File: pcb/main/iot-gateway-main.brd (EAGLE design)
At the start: 100 x 100 mm, 216 parts, among them CON2 6P-SH-TOP, CON3 2P-PH-TOP, J2 DCJACK, Q1 AO3400, Q2 AO3400, Q3 AO3400, Q4 AO3400, T5 BC817, U1 74LVC1G08, U10 CCS811, U11 LT4040, U12 LT8610, U13 LTC2942, U14 FS312F-G, U15 FS8205, U16 MIC23159, U17 ER-TFT035-6-BOT, U18 EFM32GG11B820F2048GQ100, U2 SST26VF064B, U21 74LVC1G04, U3 SST26VF016B, U4 ESP8266EX, U5 RFM69HW, U6 SIM800C, U7 SI7021, U8 SI7210, U9 BMP280, Y1 8 MHz, Y2 32.768 kHz, Y3 24 MHz

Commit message: Big changes to main schematic Finished USB/PD daughter board
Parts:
- removed C73: 100nF, Capacitor:CAP0603
- removed D31: GREEN, LED:0603
- removed D32: RED, LED:0603
- removed J2: DCJACK, DC Jack:DC-050
- removed Q4: AO3400, Alpha Omega:SOT23
- removed R110: 510 Ohms, Resistor:RES0603
- removed R111: 330 Ohms, Resistor:RES0603
- removed T5: BC817, Generic BJT:SOT23
- removed Y1: 8 MHz, Crystal:2-SMD-5032
- removed Y2: 32.768 kHz, Crystal:CM200S
- removed Y3: 24 MHz, Crystal:2-SMD-5032
- added C10, C44, C71: 100nF, Capacitor:CAP0603
- added C45: 1uF, Capacitor:CAP0603
- added C70: 22uF, Capacitor:CAP1206
- added C9: 100uF, Capacitor:CAP1206
- added CON1, CON6: 6P-SH-TOP, JST:SH-06-TOP
- added CON4: 5P-SH-TOP, JST:SH-05-TOP
- added CON5: 3P-SH-TOP, JST:SH-03-TOP
- added D5: RED, LED:1206_REV
- added D6: SMAJ24A, TVS:DO214AC
- added D7: WS2812B, LED:WS2812B-SMD5050
- added LOGO1: OSHW-LOGOM, Silkscreen:OSHW-LOGO-M
- added LOGO2: JS-5MM, Silkscreen:JS_5MM
- added R13: 10K Ohms, Resistor:RES0603
- added R56, R57, R87, R88, R91: 100K Ohms, Resistor:RES0603
- added R65: 71.5K Ohms, Resistor:RES0603
- added R89, R90: 33 Ohms, Resistor:RES0603
- added T1: BC817, Generic BJT:SOT23
- added TP10, TP11, TP12, TP9: TESTPOINT-1.27MM, PADs:PAD1.27MM
- added U19: LTC2942, Analog Devices:DFN6
- added U20: FS8205, Fortune:SOT23-6
- added X1: 8 MHz, Crystal:2-SMD-5032
- added X2: 32.768 kHz, Crystal:2-SMD-3215
- added X3: 26 MHz, Crystal:4-SMD-3225
- C11: value 1nF -> 100nF
- C12: value 100uF -> 100nF; device Capacitor:CAP1206 -> Capacitor:CAP0603
- C14: value 100nF -> 4pF
- C15: value 100nF -> 20pF
- C16: value 100nF -> 4.7pF
- C17: value 4pF -> 20pF
- C18: value 4.7pF -> 100nF
- C19: value 20pF -> 100nF
- C20: value 20pF -> 100uF; device Capacitor:CAP0603 -> Capacitor:CAP1206
- C22, C24: value 100uF -> 33pF; device Capacitor:CAP1206 -> Capacitor:CAP0603
- C23, C42, C43: value 100nF -> 1uF
- C25, C38: value 1uF -> 100nF
- C26, C27: value 33pF -> 100nF
- C29: value 100nF -> 100uF; device Capacitor:CAP0603 -> Capacitor:CAP1206
- C32: value 100uF -> 100nF; device Capacitor:AL-CAP-CASE-D -> Capacitor:CAP0603
- C33, C34: value 4.7uF -> 1nF
- C37: value 10nF -> 100nF
- C39: value 100uF -> 4.7uF; device Capacitor:CAP1206 -> Capacitor:CAP0603
- C40: value 22uF -> 4.7uF; device Capacitor:CAP1206 -> Capacitor:CAP0603
- C41: value 1nF -> 470pF
- C46: value 10pF -> 100uF; device Capacitor:CAP0603 -> Capacitor:CAP1206
- C47: value 100uF -> 10nF; device Capacitor:CAP1206 -> Capacitor:CAP0603
- C48: value 22uF -> 470pF; device Capacitor:CAP1206 -> Capacitor:CAP0603
- C49: value 10uF -> 470pF
- C50, C53, C54, C62: value 100nF -> 470pF
- C52: value 100nF -> 10pF
- C55: value 4.7uF -> 100uF; device Capacitor:CAP0603 -> Capacitor:CAP1206
- C56: value 100nF -> 10uF
- C57: value 10uF -> 22uF; device Capacitor:CAP0603 -> Capacitor:CAP1206
- C58, C59, C64, C65: value 470pF -> 100nF
- C63: device Capacitor:CAP1206 -> Capacitor:AL-CAP-CASE-D
- C66: value 470pF -> 10uF
- C67: value 470pF -> 100uF; device Capacitor:CAP0603 -> Capacitor:CAP1206
- C68: value 470pF -> 22uF; device Capacitor:CAP0603 -> Capacitor:CAP1206
- C69: value 100nF -> 22uF; device Capacitor:CAP0603 -> Capacitor:CAP1206
- C7: value 100nF -> 4.7uF
- CON2: value 6P-SH-TOP -> 2P-PH-TOP; device JST:SH-06-TOP -> JST:PH-02-TOP
- D1: value WS2812B -> BLUE; device LED:WS2812B-SMD5050 -> LED:1206_REV
- D2: value LED1206 -> WHITE; device LED:1206 -> LED:1206_REV
- D3: value LED1206 -> WS2812B; device LED:1206 -> LED:WS2812B-SMD5050
- D4: value SMAJ24A -> LED1206-REV; device TVS:DO214AC -> LED:1206_REV
- E1, E2: device Microstrip Antenna:TRACE_ANTENNA_2.4GHZ_15.2MM -> Antenna:TRACE_ANTENNA_2.4GHZ_15.2MM
- F1: device PTC Fuses:1812 -> PTC Fuses:1206
- L1: value 1.8nH -> 4.7uH
- L2: value 4.7uH -> 1.8nH; device Inductor:IND0606 -> Inductor:IND0603
- L3: value 2.2uH -> 470nH; device Inductor:IND0505 -> Inductor:IND3225
- L4: value 1uH -> 4.7uH; device Inductor:IND0805 -> Inductor:IND0606
- L5: value 470nH -> 1uH; device Inductor:IND3225 -> Inductor:IND0805
- L6: value 4.7uH -> 2.2uH; device Inductor:IND0603 -> Inductor:IND0505
- R1: value 10K Ohms -> 4.7K Ohms
- R10: value 22 Ohms -> 12K Ohms
- R11: value 1 MOhms -> 10K Ohms
- R12, R20: value 10K Ohms -> 330 Ohms
- R14: value 100 Ohms -> 10K Ohms
- R15, R8: value 100K Ohms -> 10K Ohms
- R16: value 0 Ohms -> 200 Ohms
- R18, R33, R36, R4, R6, R7: value 10K Ohms -> 100K Ohms
- R19: value 12K Ohms -> 100K Ohms
- R2: value 330 Ohms -> 4.7K Ohms
- R22, R9: value 10K Ohms -> 0 Ohms
- R23: value 200 Ohms -> 0 Ohms
- R24: value 10K Ohms -> 22 Ohms
- R25, R46: value 100K Ohms -> 22 Ohms
- R27: value 22 Ohms -> 10K Ohms
- R28: value 330 Ohms -> 10K Ohms
- R29: value 22 Ohms -> 100K Ohms
- R3: value 22 Ohms -> 4.7K Ohms
- R32: value 100K Ohms -> 0 Ohms
- R34, R35: value 0 Ohms -> 100K Ohms
- R37: value 10K Ohms -> 1 MOhms
- R38, R77, R78: value 100K Ohms -> 100 Ohms
- R39: value 25m Ohms -> 1 MOhms; device Resistor:RES1206 -> Resistor:RES0603
- R40: value 18.2K Ohms -> 100 Ohms
- R41: value 100K Ohms -> 1 MOhms
- R42: value 1M Ohms -> 100 Ohms
- R43: value 243K Ohms -> 100K Ohms
- R44: value 12m Ohms -> 1K Ohms; device Resistor:RES1206 -> Resistor:RES0603
- R45: value 1.69M Ohms -> 10K Ohms
- R47: value 100K Ohms -> 147K Ohms
- R48: value 324K Ohms -> 21K Ohms
- R49: value 2K Ohms -> 100K Ohms
- R5: value 1K Ohms -> 4.7K Ohms
- R50, R55: value 100 Ohms -> 100K Ohms
- R51: value 1 MOhms -> 100K Ohms
- R52: value 100 Ohms -> 357K Ohms
- R53: value 100 Ohms -> 61.9K Ohms
- R54: value 1 MOhms -> 17.8K Ohms
- R58: value 309K Ohms -> 100K Ohms
- R59: value 71.5K Ohms -> 100K Ohms
- R61: value 178K Ohms -> 100K Ohms
- R62: value 60.4K Ohms -> 1M Ohms
- R63: value 100K Ohms -> 232K Ohms
- R64: value 0 Ohms -> 309K Ohms
- R66: value 100K Ohms -> 510 Ohms
- R67: value 100K Ohms -> 178K Ohms
- R68: value 1K Ohms -> 60.4K Ohms
- R70: value 100K Ohms -> 330 Ohms
- R73: value 357K Ohms -> 100K Ohms
- R74: value 61.9K Ohms -> 2K Ohms
- R76: value 100K Ohms -> 10m Ohms; device Resistor:RES0603 -> Resistor:RES1206
- R79: value 21K Ohms -> 100K Ohms
- R80: value 147K Ohms -> 1.5M Ohms
- R81: value 100K Ohms -> 274K Ohms
- R82: value 100K Ohms -> 25m Ohms; device Resistor:RES0603 -> Resistor:RES1206
- R84, R85: value 100K Ohms -> 4.7K Ohms
- U1: value 74LVC1G08 -> SST26VF064B; device Logic:SC70-5 -> Microchip:WSOIC8
- U10: value CCS811 -> BMP280; device AMS:LGA10 -> Bosch:BMP280
- U11: value LT4040 -> CCS811; device Analog Devices:QFN24_ASYM -> AMS:LGA10
- U12: value LT8610 -> ER-TFT035-6-BOT; device Analog Devices:MSOP16_EP -> BuyDisplay:FPC-50P-TFT-BOT
- U13: value LTC2942 -> 74LVC1G17; device Analog Devices:DFN6 -> Logic:SC70-5
- U14: value FS312F-G -> LT8636; device Fortune:SOT23-6 -> Analog Devices:QFN20_ASYM_CORNER
- U15: value FS8205 -> MIC23159; device Fortune:SOT23-6 -> Microchip:VQFN20
- U16: value MIC23159 -> 74LVC1G04; device Microchip:VQFN20 -> Logic:SC70-5
- U17: value ER-TFT035-6-BOT -> LTC4040; device BuyDisplay:FPC-50P-TFT-BOT -> Analog Devices:QFN24_ASYM
- U18: value EFM32GG11B820F2048GQ100 -> FS312F-G; device EFM32:QFP100 -> Fortune:SOT23-6
- U2: value SST26VF064B -> EFM32GG11B820F2048GQ100; device Microchip:WSOIC8 -> EFM32:QFP100
- U21: value 74LVC1G04 -> LTC4313-1; device Logic:SC70-5 -> Analog Devices:DFN8
- U6: value SIM800C -> 74LVC1G08; device SimCom:SIM800C -> Logic:SC70-5
- U7: value SI7021 -> SIM800C; device Silicon Labs:DFN6 -> SimCom:SIM800C
- U8: value SI7210 -> SI7021; device Silicon Labs:SOT23-5 -> Silicon Labs:DFN6
- U9: value BMP280 -> SI7210; device Bosch:BMP280 -> Silicon Labs:SOT23-5
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- renumbered U$1 to LOGO3
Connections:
- removed net 12V0: C32.1, C33.1, C36.1, D4.C, F1.1, R80.2, U12.4, U12.5, U12.6
- removed net 12V0_UNFUSED: F1.2, J2.C, J2.C'
- removed net 12V0_VSENSE: C64.1, R79.2, R80.1
- removed net 5V0_NBU_NSENS_SYNC: R78.2, U12.1
- removed net I2C1_SCL_TFT: R7.1, U17.44
- removed net I2C1_SDA_TFT: R6.1, U17.45
- removed net US1_CLK_TFT: U17.36
- removed net US1_CS_TFT: R66.1, U17.38
- removed net US1_MISO_TFT: U17.33
- removed net US1_MOSI_TFT: U17.34
- removed net US2_CTS_GSM: U6.4
- removed net US2_RTS_GSM: U6.3
- removed net US2_RX_GSM: U6.1
- removed net US2_TX_GSM: U6.2
- removed net VIN_DET: J2.DT, R41.1
- removed net WIFI_XTAL_IN: C19.2, U4.28, Y3.1
- removed net WIFI_XTAL_OUT: C20.2, U4.27, Y3.2
- new net !BAT_CHRG_EN: R88.1, U17.4
- new net !FUEL_GAUGE_IRQ: R79.1, U19.5
- new net !US2_CS_TFT: R34.1, U12.38
- new net !USB_PD_IRQ: CON6.2, R83.1
- new net !USB_VBUS_HV_EN: CON4.3
- new net DCJACK_DET: CON6.5, R69.1
- new net I2C1_SCL_SYS: R5.1, U12.44, U19.3, U21.3
- new net I2C1_SDA_SYS: R3.1, U12.45, U19.4, U21.6
- new net I2C_SCL_USB_PD: CON6.3, R85.1, U21.2
- new net I2C_SDA_USB_PD: CON6.4, R84.1, U21.7
- new net N$32: TP11.TP, U7.12
- new net N$55: TP10.TP, U7.11
- new net N$56: TP8.TP, U7.10
- new net N$60: TP5.TP, U7.9
- new net N$61: C15.1, U4.28, X3.2
- new net N$62: C17.1, U4.27, X3.4
- new net N$63: CON5.2, R90.2
- new net N$64: CON5.1, R89.2
- new net U0_CTS_GSM: U7.4
- new net U0_RTS_GSM: U7.3
- new net U0_RX_GSM: U7.1
- new net U0_TX_GSM: U7.2
- new net US2_CLK_TFT: U12.36
- new net US2_MISO_TFT: U12.33
- new net US2_MOSI_TFT: U12.34
- new net USB_D+: R89.1
- new net USB_D-: R90.1
- new net USB_PD_I2C_EN: R87.2, U21.1
- new net USB_PD_I2C_READY: R86.1, U21.5
- new net USB_VBUS_HV_STAT: CON4.2, R91.1
- new net USB_VBUS_SUP_EN: CON4.4
- new net VIN: C40.1, C42.1, C43.1, C63.1, D6.C, F1.1, R47.2, U14.11, U14.14, U14.6
- new net VIN_UNFUSED: CON3.1, F1.2
- new net VIN_VSENSE: C41.1, R47.1, R48.2
- net !5V0_BACKUP: now also R71.1, U16.2, U17.20; no longer R72.1, U11.20, U21.2
- net !BAT_CHRG: now also R75.1, U17.8; no longer R63.1, U11.8
- net !BAT_FAULT: now also R73.1, U17.9; no longer R67.1, U11.9
- net !CCS811_IRQ: now also R29.1, U11.3; no longer R38.1, U10.3
- net !CCS811_RESET: now also R27.1, U11.2; no longer R36.1, U10.2
- net !CCS811_WAKE: now also R28.1, U11.7; no longer R37.1, U10.7
- net !GSM_DTR: now also U7.6; no longer U6.6
- net !GSM_RING: now also U7.7; no longer U6.7
- net !RESET: now also R6.1, U2.36; no longer R69.1, U18.36
- net !TFT_RESET: now also R33.1, U12.10; no longer R32.1, U17.10
- net !TFT_TOUCH_IRQ: now also R36.1, U12.46; no longer R47.1, U17.46
- net !TFT_TOUCH_RESET: now also R35.1, U12.47; no longer R46.1, U17.47
- net !UI_BTN1: now also C33.1, R37.1, R38.2; no longer C41.1, R54.1, R55.2
- net !UI_BTN2: now also C34.1, R39.1, R40.2; no longer C35.1, R51.1, R52.2
- net !UI_BTN3: now also C35.1, R41.1, R42.2; no longer C11.1, R11.1, R14.2
- net !WIFI_RESET: now also CON1.1, R11.1; no longer CON2.1, R18.1
- net 1V8: now also C7.1, L1.1, U2.58; no longer C34.1, L6.1, U18.58
- net 3V3: now also C10.1, C11.1, C18.1, C25.1, C26.1, C27.1, C32.1, C56.1, C61.1, C71.1, C9.1, CON6.1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; no longer C14.1, C15.1, C16.1, C22.1, C52.1, C53.1, C54.1, C57.1, C73.1, L4.2, R15.2, R20.2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
- net 3V3_FB: now also R64.1, R65.2, U15.11; no longer R58.1, R59.2, U16.11
- net 3V3_PGOOD: now also R59.1, U15.12; no longer R60.1, U16.12
- net 4V2: now also C19.1, C20.1, C44.1, C46.1, L3.1, R50.2, R52.2, U15.17, U7.34, U7.35; no longer C23.1, C24.1, C62.1, C63.1, L5.1, R73.2, R82.2, U16.17, U6.34, U6.35
- net 4V2_EN: now also R49.2, U15.18; no longer R76.2, U16.18
- net 4V2_FB: now also R52.1, R53.2, U15.16; no longer R73.1, R74.2, U16.16
- net 4V2_PGOOD: now also R56.1, U15.15; no longer R75.1, U16.15
- net 4V2_VSENSE: now also C48.1, R50.1, R51.2; no longer C65.1, R81.2, R82.1
- net 5V0: now also C36.1, C37.1, C38.1, C39.1, C58.1, C67.1, C68.1, C70.1, CON4.1, D3.1, D7.1, Q3.3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; no longer C47.1, C48.1, C55.1, C56.1, C61.1, C7.1, D1.1, Q1.3, R45.2, R5.2, R84.2, U11.1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
- net 5V0_FB: now also R80.1, R81.2, U17.10, U17.18; no longer R45.1, R48.2, U11.10, U11.18
- net 5V0_ISENSE: now also C62.1, U17.3; no longer C68.1, U11.3
- net 5V0_NBU: now also Q3.2, R76.1, U17.7; no longer Q1.2, R44.1, U11.7
- net 5V0_NBU_NSENS: now also C52.1, C55.1, C57.1, C59.1, L4.2, R62.2, R66.2, R67.2, R76.2, U14.2, U17.16, U17.6; no longer C39.1, C40.1, C42.1, C46.1, L2.2, R110.2, R42.2, R44.2, R61.2, U11.16, U11.6, U12.14
- net 5V0_NBU_NSENS_FB: now also C52.2, R62.1, R63.2, U14.19, U14.20; no longer C46.2, R42.1, R43.2, U12.16
- net 5V0_NBU_NSENS_PGOOD: now also R55.1, U14.1; no longer R77.1, U12.15
- net 5V0_PGOOD: now also R72.1, U17.11; no longer R71.1, U11.11
- net 5V0_VSENSE: now also C50.1, R57.1, R58.2; no longer C66.1, R83.2, R84.1
- net GBAT: now also C64.2, CON2.2, U18.6, U19.2, U20.3; no longer C51.2, CON3.2, U13.2, U14.6, U15.3
- net GND: now also C10.2, C14.1, C16.1, C17.2, C18.2, C19.2, C20.2, C43.2, C44.2, C45.2, C46.2, C70.2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; no longer C14.2, C16.2, C17.1, C18.1, C19.1, C20.1, C52.2, C64.2, C73.2, CON2.6, D1.3, D31.1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
- net GSM_LED_EN: now also U6.2; no longer U1.2
- net GSM_PWRKEY: now also R21.2; no longer R33.2
- net GSM_RF_SYNC: now also U7.29; no longer U6.29
- net GSM_STATUS: now also U7.42; no longer U6.42
- net I2C0_SCL_SENS: now also R2.1, U10.4, U11.10, U8.6, U9.3; no longer R4.1, U10.10, U7.6, U8.3, U9.4
- net I2C0_SDA_SENS: now also U10.3, U11.9, U9.1; no longer U10.9, U7.1, U9.3
- net LED_DI: now also R43.2, U13.2; no longer R10.2
- net MAG_ALERT: now also U9.5; no longer U8.5
- net MAIN_HFXTAL_N: now also X1.1; no longer Y1.1
- net MAIN_HFXTAL_P: now also X1.2; no longer Y1.2
- net MAIN_LFXTAL_N: now also X2.2; no longer Y2.4
- net MAIN_LFXTAL_P: now also X2.1; no longer Y2.1
- net N$1: now also U11.4, U11.5; no longer U10.4, U10.5
- net N$10: now also R9.1; no longer R16.1
- net N$12: now also R54.2, U14.17; no longer R40.2, U12.3
- net N$13: now also C47.1, U14.18; no longer C37.1, U12.2
- net N$14: now also C45.1, U14.15, U14.3; no longer C38.1, U12.13
- net N$15: now also C51.1, L4.1, U14.10, U14.8, U14.9; no longer C43.1, L2.1, U12.10, U12.11, U12.9
- net N$16: now also D2.C, R20.2; no longer D2.1, R28.2
- net N$17: now also D2.A, U6.4; no longer D2.2, U1.4
- net N$18: now also R26.1; no longer R27.1
- net N$19: now also D3.4, U13.4; no longer D1.4, Q4.3, R5.1
- net N$2: now also U7.32; no longer U6.32
- net N$20: now also R22.1, R23.2, U7.20; no longer R34.1, R35.2, U6.20
- net N$21: now also R22.2; no longer R34.2
- net N$22: now also R23.1; no longer R35.1
- net N$23: now also TP1.TP, U7.28; no longer TP8.TP, U6.28
- net N$24: now also Q1.1; no longer Q3.1
- net N$25: now also TP9.TP, U7.26; no longer TP1.TP, U6.26
- net N$26: now also TP6.TP, U7.25; no longer TP2.TP, U6.25
- net N$27: now also T1.3, U7.39; no longer T5.3, U6.39
- net N$28: now also R21.1, T1.1; no longer R33.1, T5.1
- net N$29: now also D1.C, R12.2; no longer D3.1, R2.2
- net N$3: now also R25.1; no longer R26.1
- net N$30: now also U7.24; no longer U6.24
- net N$31: now also TP2.TP, U7.40; no longer TP5.TP, U6.40
- net N$33: now also Q1.3, R32.1; no longer Q3.3, R64.1
- net N$34: now also R45.2, R46.2; no longer R3.2, R9.2
- net N$35: now also R44.1; no longer R68.1
- net N$36: now also C51.2, U14.7; no longer C43.2, U12.12
- net N$37: now also Q3.1, U17.15; no longer Q1.1, U11.15
- net N$38: now also L6.1, U17.21, U17.22; no longer L3.1, U11.21, U11.22
- net N$39: now also R24.2; no longer R29.2
- net N$4: now also U6.1, U7.41; no longer U1.1, U6.41
- net N$40: now also R74.2, U17.2; no longer R49.2, U11.2
- net N$41: now also R77.1, U18.5; no longer R50.1, U14.5
- net N$42: now also R78.2, U18.2; no longer R53.2, U14.2
- net N$43: now also U18.3, U20.6; no longer U14.3, U15.6
- net N$44: now also U18.1, U20.4; no longer U14.1, U15.4
- net N$46: now also L5.1, U15.4; no longer L4.1, U16.4
- net N$47: now also C53.1, U15.13; no longer C58.1, U16.13
- net N$48: now also C49.1, U15.14; no longer C59.1, U16.14
- net N$49: now also L3.2, U15.3; no longer L5.2, U16.3
- net N$5: now also R10.2; no longer R19.1
- net N$50: now also L1.2, U2.56; no longer L6.2, U18.56
- net N$51: now also TP7.TP, U7.23; no longer TP6.TP, U6.23
- net N$52: now also D3.2, D7.4; no longer Q4.1, R10.1, R12.2
- net N$53: now also R40.1; no longer R52.1
- net N$54: now also R32.2, U12.2, U12.3; no longer R64.2, U17.2, U17.3
- net N$57: now also R42.1; no longer R14.1
- net N$58: now also TP4.TP, U7.22; no longer TP7.TP, U6.22
- net N$59: now also R38.1; no longer R55.1
- net N$6: now also R16.2; no longer R23.2
- net N$7: now also C16.2, L2.2, R9.2; no longer C18.2, L1.2, R16.2
- net N$8: now also C14.2, L2.1; no longer C17.2, L1.1
- net N$9: now also U2.60; no longer U18.60
- net N$90: now also R70.2, U16.4; no longer R111.2, U21.4
- net N$91: now also D4.A, R66.1; no longer D31.2, R110.1
- net N$92: now also D5.A, R70.1; no longer D32.2, R111.1
- net PF_THRESH: now also R67.1, R68.2, U17.19; no longer R61.1, R62.2, U11.19
- net QSPI_CLK: now also U1.6, U2.84; no longer U18.84, U2.6
- net QSPI_CS0: now also R4.1, U1.1, U2.85; no longer R8.1, U18.85, U2.1
- net QSPI_D0: now also U1.5, U2.88; no longer U18.88, U2.5
- net QSPI_D1: now also U1.2, U2.89; no longer U18.89, U2.2
- net QSPI_D2: now also U1.3, U2.90; no longer U18.90, U2.3
- net QSPI_D3: now also U1.7, U2.91; no longer U18.91, U2.7
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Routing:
- removed copper zone on layer 1, net KEEPOUT
- removed copper zone on layer 16, net KEEPOUT1
- removed copper zone on layer 1, net KEEPOUT2
- removed copper zone on layer 16, net KEEPOUT3
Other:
- board size 100 x 100 mm -> 150 x 100 mm
- board text added: "IoT Gateway v2 Jan 2020"
- board text removed: "Designed and assembled in Portugal"
- board text removed: "IoT Gateway v1 Mar 2019"

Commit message: Place everything important inside the board space and start routing
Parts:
- added C72: 10uF, Capacitor:CAP0603
- added C73: 100nF, Capacitor:CAP0603
- added C74: 22uF, Capacitor:CAP1206
- added D8: SP0502BAJT, TVS:SC70-3
- C29: value 100uF -> 10uF; device Capacitor:CAP1206 -> Capacitor:CAP0603
- C56: value 10uF -> 100nF
- C63: value 100uF -> 10uF; device Capacitor:AL-CAP-CASE-D -> Capacitor:CAP1206
- LOGO2: value JS-5MM -> JS-10MM; device Silkscreen:JS_5MM -> Silkscreen:JS_10MM
- X1: value 8 MHz -> 24 MHz
- moved R91 463.1 mm to (26.1, 117.2), turned to 90 degrees
- moved R88 457.7 mm to (24.3, 117.2), turned to 90 degrees
- moved CON4 438.2 mm to (59.3, 97.1)
- moved R90 422.4 mm to (40.9, 91.0), turned to 90 degrees
- moved R89 418.1 mm to (42.7, 91.0), turned to 90 degrees
- moved C71 407.2 mm to (50.5, 86.5), turned to 90 degrees
- moved C70 404.0 mm to (59.8, 92.0), turned to 180 degrees
- moved R86 398.1 mm to (18.8, 117.2), turned to 90 degrees
- moved R87 396.5 mm to (45.3, 82.3), turned to 90 degrees
- moved C69 391.7 mm to (50.7, 92.0), turned to 180 degrees
- moved R83 383.3 mm to (22.5, 117.2), turned to 90 degrees
- moved R69 377.9 mm to (20.7, 117.2), turned to 90 degrees
- moved R85 372.7 mm to (48.7, 86.5), turned to 270 degrees
- moved U21 372.3 mm to (50.5, 81.9)
- moved R84 369.4 mm to (52.3, 86.5), turned to 270 degrees
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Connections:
- net N$1 renamed CCS811_HEATER_PWM
- net N$10 renamed WIFI_ANT_EXT
- net N$11 renamed WIFI_IO16
- net N$12 renamed 5V0_NBU_NSENS_RT
- net N$13 renamed 5V0_NBU_NSENS_SS
- net N$14 renamed 5V0_NBU_NSENS_INTVCC
- net N$15 renamed 5V0_NBU_NSENS_SW
- net N$17 renamed GSM_LED
- net N$18 renamed SIM_CLK_FILT
- net N$19 renamed LED_DI_BUF
- net N$2 renamed GSM_ANT
- net N$20 renamed BT_ANT
- net N$21 renamed BT_ANT_INT
- net N$22 renamed BT_ANT_EXT
- net N$23 renamed GSM_VRTC
- net N$25 renamed GSM_USB_D-
- net N$26 renamed GSM_USB_D+
- net N$27 renamed !GSM_PWRKEY
- net N$3 renamed SIM_RST_FILT
- net N$30 renamed GSM_USB_VBUS
- net N$31 renamed GSM_2V8
- net N$32 renamed GSM_SPK-
- net N$33 renamed TFT_BACKLIGHT_DRIVER
- net N$35 renamed BUZZ_DRV
- net N$36 renamed 5V0_NBU_NSENS_BST
- net N$38 renamed VBAT_SW
- net N$39 renamed SIM_DATA_FILT
- net N$4 renamed GSM_NETLIGHT
- net N$40 renamed BAT_CHRG_PROG
- net N$41 renamed BAT_PROT_VCC
- net N$42 renamed BAT_PROT_CS
- net N$43 renamed BAT_OC
- net N$44 renamed BAT_OD
- net N$46 renamed 3V3_SW
- net N$47 renamed 3V3_SS
- net N$48 renamed 4V2_SS
- net N$49 renamed 4V2_SW
- net N$5 renamed WIFI_BIAS
- net N$50 renamed MAIN_VREG_SW
- net N$51 renamed GSM_UART2_RX
- net N$52 renamed LED_DO
- net N$54 renamed TFT_BACKLIGHT_PWM
- net N$55 renamed GSM_SPK+
- net N$56 renamed GSM_MIC-
- net N$58 renamed GSM_UART2_TX
- net N$6 renamed WIFI_QSPI_CLK_FILT
- net N$60 renamed GSM_MIC+
- net N$61 renamed WIFI_XTAL_IN
- net N$62 renamed WIFI_XTAL_OUT
- net N$7 renamed WIFI_ANT
- net N$8 renamed WIFI_ANT_FILT
- net N$9 renamed MAIN_VDD_CORE
- net N$90 renamed 5V0_BACKUP
- net !UI_BTN1: now also C34.1, R39.1, R40.2; no longer C33.1, R37.1, R38.2
- net !UI_BTN2: now also C33.1, R37.1, R38.2; no longer C34.1, R39.1, R40.2
- net 3V3: now also C72.1, C74.1
- net 5V0: now also C73.1
- net GBAT: no longer U19.2
- net GND: now also C72.2, C73.2, C74.2, D8.3, U19.2
- net MAIN_HFXTAL_N: now also U2.43, X1.2; no longer X1.1
- net MAIN_HFXTAL_P: now also U2.42, X1.1; no longer X1.2
- net MAIN_LFXTAL_N: now also U2.25
- net MAIN_LFXTAL_P: now also U2.24
- net USB_D+: now also D8.1, U2.75
- net USB_D-: now also D8.2, U2.74
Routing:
- net 5V0: track 0.00 -> 142.4 mm, vias 0 -> 7
- net 4V2: track 0.00 -> 139.0 mm, vias 0 -> 5
- net 5V0_NBU_NSENS: track 0.00 -> 97.5 mm, vias 0 -> 5
- net 3V3: track 0.00 -> 49.8 mm, vias 0 -> 2
- net VBAT: track 0.00 -> 47.7 mm, vias 0 -> 2
- net VIN: track 0.00 -> 40.6 mm, vias 0 -> 3
- net 5V0_FB: track 0.00 -> 27.3 mm, vias 0 -> 3
- net QSPI_CS0: track 0.00 -> 21.7 mm, vias 0 -> 2
- net I2C_SDA_USB_PD: track 0.00 -> 21.1 mm, vias 0 -> 3
- net 5V0_NBU: track 0.00 -> 19.5 mm, vias 0 -> 2
- net I2C_SCL_USB_PD: track 0.00 -> 17.5 mm, vias 0 -> 3
- net GBAT: track 0.00 -> 17.2 mm, vias 0 -> 3
- net QSPI_D3: track 0.00 -> 17.1 mm, vias 0 -> 2
- net QSPI_D1: track 0.00 -> 15.9 mm
- net QSPI_CLK: track 0.00 -> 14.7 mm, vias 0 -> 2
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- added copper zone on layer 1, net 5V0
- added copper zone on layer 1, net 5V0_NBU_NSENS_SW
- added copper zone on layer 1, net VBAT_SW

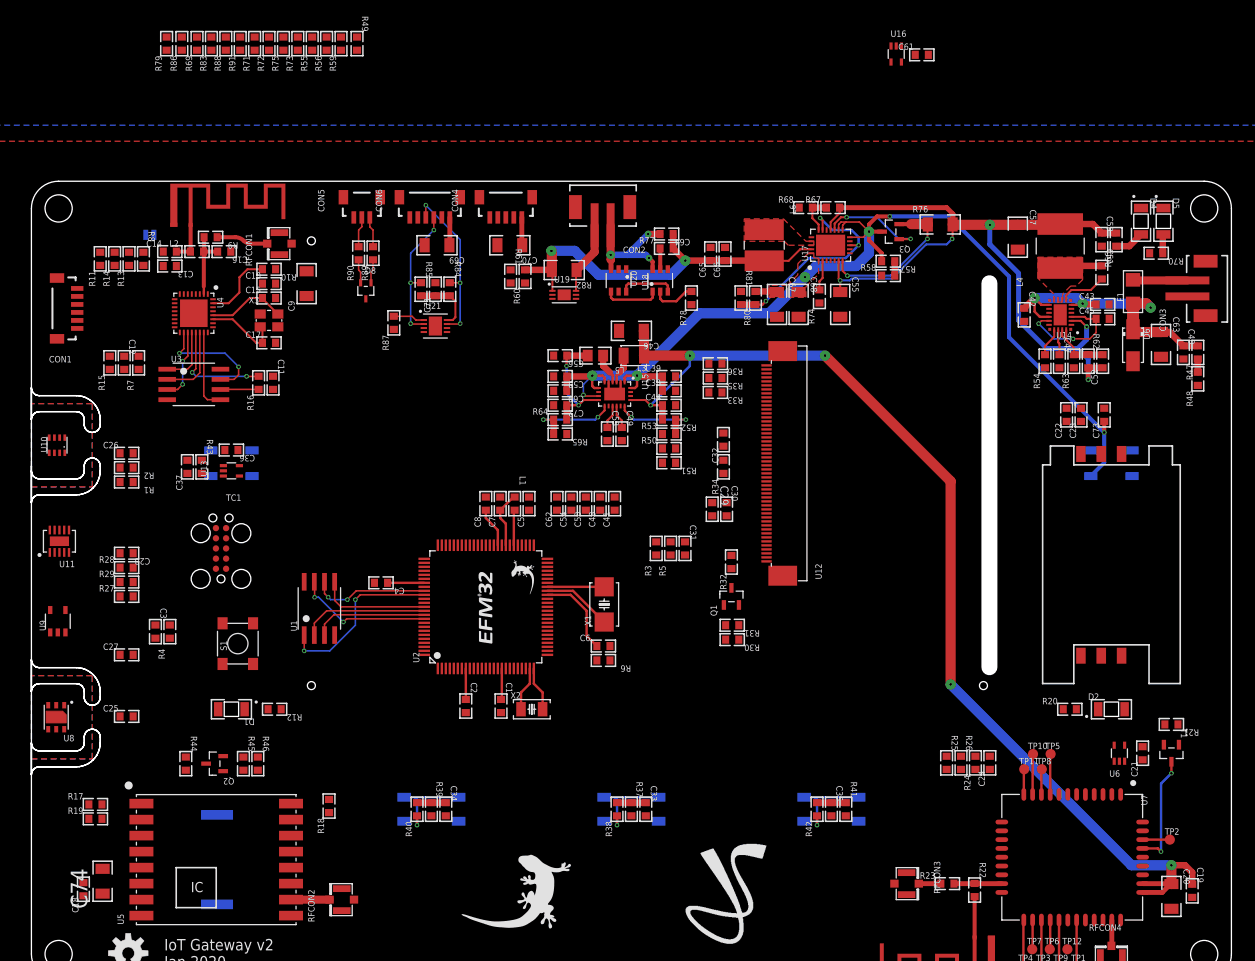
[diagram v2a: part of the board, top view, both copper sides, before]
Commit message: Connect IOs to MCU
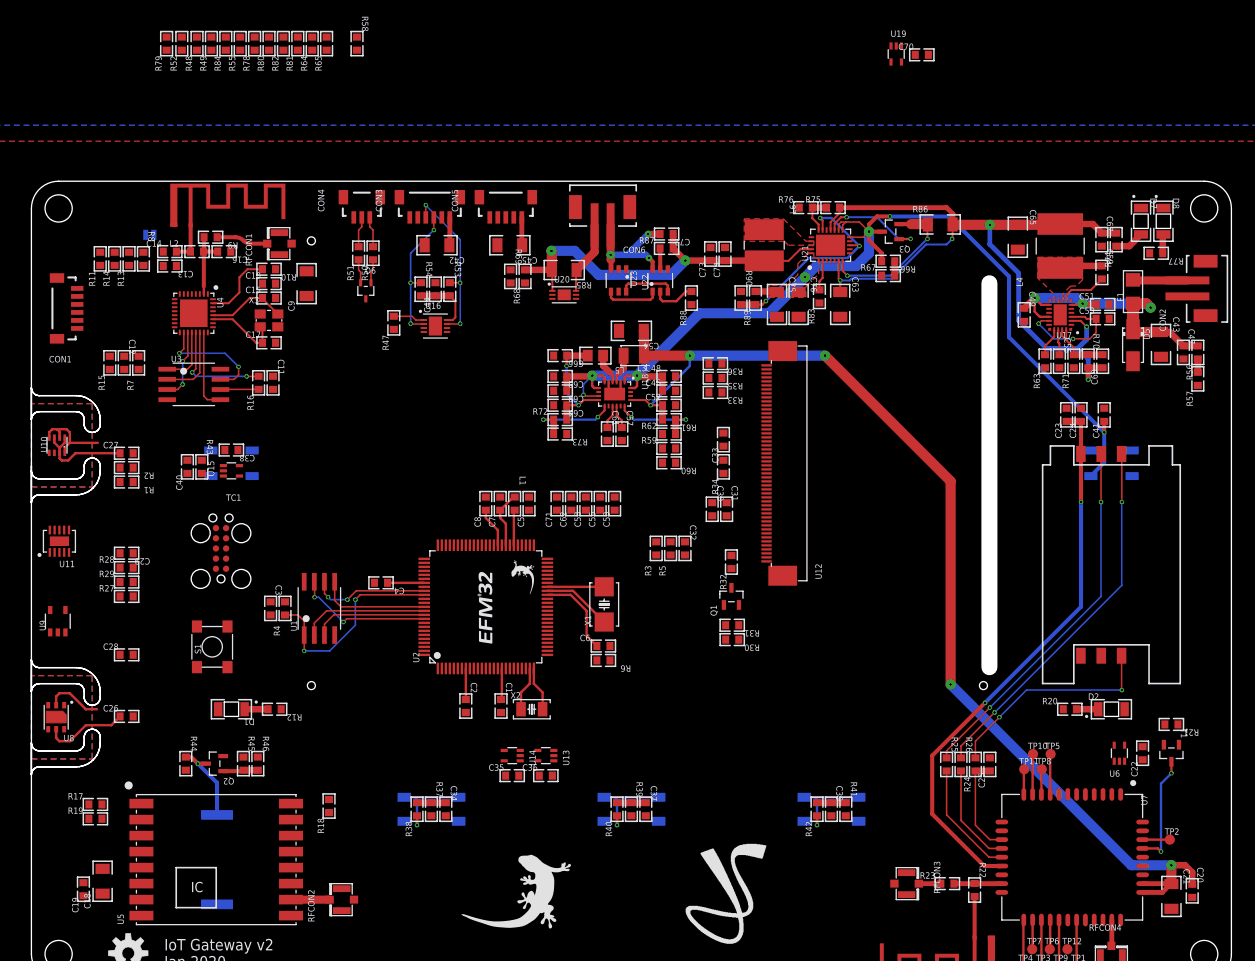
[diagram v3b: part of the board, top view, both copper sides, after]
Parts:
- removed R91: 100K Ohms, Resistor:RES0603
- added C75: 100uF, Capacitor:CAP1206
- added C76: 22uF, Capacitor:CAP1206
- added U22: FS312F-G, Fortune:SOT23-6
- added U23: FS8205, Fortune:SOT23-6
- C18, C65: value 100nF -> 22uF; device Capacitor:CAP0603 -> Capacitor:CAP1206
- C20, C46, C67: value 100uF -> 100nF; device Capacitor:CAP1206 -> Capacitor:CAP0603
- C21: value 100nF -> 100uF; device Capacitor:CAP0603 -> Capacitor:CAP1206
- C22: value 33pF -> 100nF
- C23: value 1uF -> 33pF
- C24: value 33pF -> 1uF
- C25: value 100nF -> 33pF
- C29, C66, C72: value 10uF -> 100nF
- C30, C64: value 100nF -> 10uF
- C33, C35: value 1nF -> 100nF
- C37: value 100nF -> 1nF
- C39: value 4.7uF -> 1nF
- C40: value 4.7uF -> 100nF
- C41: value 470pF -> 100nF
- C42, C45: value 1uF -> 22uF; device Capacitor:CAP0603 -> Capacitor:CAP1206
- C43: value 1uF -> 10uF; device Capacitor:CAP0603 -> Capacitor:CAP1206
- C47: value 10nF -> 4.7uF
- C48: value 470pF -> 4.7uF
- C49, C53: value 470pF -> 1uF
- C51: value 100nF -> 1uF
- C52: value 10pF -> 100nF
- C54: value 470pF -> 100uF; device Capacitor:CAP0603 -> Capacitor:CAP1206
- C55: value 100uF -> 10nF; device Capacitor:CAP1206 -> Capacitor:CAP0603
- C56, C58, C61, C71: value 100nF -> 470pF
- C57: value 22uF -> 470pF; device Capacitor:CAP1206 -> Capacitor:CAP0603
- C60: value 4.7uF -> 10pF
- C63: value 10uF -> 100uF
- C68, C70: value 22uF -> 100nF; device Capacitor:CAP1206 -> Capacitor:CAP0603
- C69: value 22uF -> 4.7uF; device Capacitor:CAP1206 -> Capacitor:CAP0603
- C74: value 22uF -> 10uF; device Capacitor:CAP1206 -> Capacitor:CAP0603
- CON3: value 2P-PH-TOP -> 6P-SH-TOP; device JST:PH-02-TOP -> JST:SH-06-TOP
- CON4: value 5P-SH-TOP -> 3P-SH-TOP; device JST:SH-05-TOP -> JST:SH-03-TOP
- CON5: value 3P-SH-TOP -> 5P-SH-TOP; device JST:SH-03-TOP -> JST:SH-05-TOP
- CON6: value 6P-SH-TOP -> 2P-PH-TOP; device JST:SH-06-TOP -> JST:PH-02-TOP
- D4: value LED1206-REV -> WS2812B; device LED:1206_REV -> LED:WS2812B-SMD5050
- D5: value RED -> SMAJ24A; device LED:1206_REV -> TVS:DO214AC
- D6: value SMAJ24A -> SP0502BAJT; device TVS:DO214AC -> TVS:SC70-3
- D7: value WS2812B -> LED1206-REV; device LED:WS2812B-SMD5050 -> LED:1206_REV
- D8: value SP0502BAJT -> RED; device TVS:SC70-3 -> LED:1206_REV
- R47: value 147K Ohms -> 100K Ohms
- R48: value 21K Ohms -> 100K Ohms
- R50, R51: value 100K Ohms -> 33 Ohms
- R52: value 357K Ohms -> 100K Ohms
- R53: value 61.9K Ohms -> 4.7K Ohms
- R54: value 17.8K Ohms -> 4.7K Ohms
- R56: value 100K Ohms -> 147K Ohms
- R57: value 100K Ohms -> 21K Ohms
- R61: value 100K Ohms -> 357K Ohms
- R62: value 1M Ohms -> 61.9K Ohms
- R63: value 232K Ohms -> 17.8K Ohms
- R64: value 309K Ohms -> 100K Ohms
- R65: value 71.5K Ohms -> 100K Ohms
- R66: value 510 Ohms -> 100K Ohms
- R67: value 178K Ohms -> 100K Ohms
- R68: value 60.4K Ohms -> 100K Ohms
- R70: value 330 Ohms -> 1M Ohms
- R71: value 100K Ohms -> 232K Ohms
- R72: value 100K Ohms -> 309K Ohms
- R73: value 100K Ohms -> 71.5K Ohms
- R74: value 2K Ohms -> 510 Ohms
- R75: value 100K Ohms -> 178K Ohms
- R76: value 10m Ohms -> 60.4K Ohms; device Resistor:RES1206 -> Resistor:RES0603
- R77: value 100 Ohms -> 330 Ohms
- R78: value 100 Ohms -> 100K Ohms
- R80: value 1.5M Ohms -> 100K Ohms
- R81: value 274K Ohms -> 100K Ohms
- R82: value 25m Ohms -> 100K Ohms; device Resistor:RES1206 -> Resistor:RES0603
- R83: value 100K Ohms -> 2K Ohms
- R84: value 4.7K Ohms -> 100K Ohms
- R85: value 4.7K Ohms -> 25m Ohms; device Resistor:RES0603 -> Resistor:RES1206
- R86: value 100K Ohms -> 10m Ohms; device Resistor:RES0603 -> Resistor:RES1206
- R87, R88: value 100K Ohms -> 100 Ohms
- R89: value 33 Ohms -> 1.5M Ohms
- R90: value 33 Ohms -> 274K Ohms
- U13: value 74LVC1G17 -> 74LVC1G08
- U14: value LT8636 -> 74LVC1G08; device Analog Devices:QFN20_ASYM_CORNER -> Logic:SC70-5
- U15: value MIC23159 -> 74LVC1G17; device Microchip:VQFN20 -> Logic:SC70-5
- U16: value 74LVC1G04 -> LTC4313-1; device Logic:SC70-5 -> Analog Devices:DFN8
- U17: value LTC4040 -> LT8636; device Analog Devices:QFN24_ASYM -> Analog Devices:QFN20_ASYM_CORNER
- U18: value FS312F-G -> MIC23159; device Fortune:SOT23-6 -> Microchip:VQFN20
- U19: value LTC2942 -> 74LVC1G04; device Analog Devices:DFN6 -> Logic:SC70-5
- U20: value FS8205 -> LTC2942; device Fortune:SOT23-6 -> Analog Devices:DFN6
- U21: value LTC4313-1 -> LTC4040; device Analog Devices:DFN8 -> Analog Devices:QFN24_ASYM
- moved C19 138.6 mm to (6.50, 11.5), turned to 90 degrees
- moved R48 131.9 mm to (20.7, 117.2)
- moved C40 125.3 mm to (19.5, 64.3), turned to 90 degrees
- moved R56 115.5 mm to (145.8, 78.6)
- moved C74 110.5 mm to (86.7, 90.9)
- moved R71 109.8 mm to (130.3, 77.5)
- moved C25 108.1 mm to (119.8, 27.1), turned to 90 degrees
- moved R47 100.6 mm to (45.3, 82.3)
- moved D8 100.1 mm to (141.5, 95.0), turned to 270 degrees
- moved R86 97.5 mm to (113.6, 94.6), turned to 0 degrees
- moved CON3 97.3 mm to (49.8, 97.1), turned to 0 degrees
- moved D6 96.1 mm to (41.8, 86.3), turned to 180 degrees
- moved U14 87.9 mm to (60.1, 28.2), turned to 90 degrees
- moved R83 82.3 mm to (98.5, 85.6)
- moved R54 78.5 mm to (48.7, 86.5), turned to 270 degrees
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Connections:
- removed net 3V3_PGOOD: R59.1, U15.12
- removed net I2C0_SCL_SENS: R2.1, U10.4, U11.10, U8.6, U9.3
- removed net I2C0_SDA_SENS: R1.1, U10.3, U11.9, U8.1, U9.1
- removed net I2C1_SCL_SYS: R5.1, U12.44, U19.3, U21.3
- removed net I2C1_SDA_SYS: R3.1, U12.45, U19.4, U21.6
- removed net LED_DI: R43.2, U13.2
- removed net US0_CS_WIFI: R15.2, U4.13
- removed net US3_CS_RFM: R18.1, U5.15
- removed net WTIM2_CC1_TFT_BL: R30.1
- new net !UI_BTN_IRQ: U14.4, U2.10
- new net !US0_CS_WIFI: R15.2, U2.68, U4.13
- new net !US3_CS_RFM: R18.1, U2.4, U5.15
- new net I2C0_SCL_SYS: R5.1, U12.44, U16.3, U2.65, U20.3
- new net I2C0_SDA_SYS: R3.1, U12.45, U16.6, U2.64, U20.4
- new net I2C1_SCL_SENS: R2.1, U10.4, U11.10, U2.23, U8.6, U9.3
- new net I2C1_SDA_SENS: R1.1, U10.3, U11.9, U2.22, U8.1, U9.1
- new net N$1: U13.4, U14.2
- new net TIM4_CC2_LED_DI: R43.2, U15.2, U2.80
- new net WTIM2_CC2_TFT_BL: R30.1, U2.30
- net !5V0_BACKUP: now also R78.1, U19.2, U2.54, U21.20; no longer R71.1, U16.2, U17.20
- net !BAT_CHRG: now also R82.1, U2.52, U21.8; no longer R75.1, U17.8
- net !BAT_CHRG_EN: now also R84.1, U2.53, U21.4; no longer R88.1, U17.4
- net !BAT_FAULT: now also R81.1, U2.51, U21.9; no longer R73.1, U17.9
- net !CCS811_IRQ: now also U2.97
- net !CCS811_RESET: now also U2.98
- net !CCS811_WAKE: now also U2.96
- net !FUEL_GAUGE_IRQ: now also U2.94, U20.5; no longer U19.5
- net !GSM_DTR: now also U2.20
- net !GSM_RING: now also U2.19
- net !TFT_RESET: now also U2.35
- net !TFT_TOUCH_IRQ: now also U2.33
- net !TFT_TOUCH_RESET: now also U2.34
- net !UI_BTN1: now also R37.1, R38.2, U13.2, U2.11; no longer R39.1, R40.2
- net !UI_BTN2: now also C37.1, R39.1, R40.2, U13.1, U2.12; no longer C33.1, R37.1, R38.2
- net !UI_BTN3: now also C39.1, U14.1, U2.13; no longer C35.1
- net !US2_CS_TFT: now also U2.29
- net !USB_PD_IRQ: now also CON3.2, R49.1, U2.61; no longer CON6.2, R83.1
- net !USB_VBUS_HV_EN: now also CON5.3, U2.87; no longer CON4.3
- net !WIFI_RESET: now also U2.81
- net 3V3: now also C19.1, C22.1, C33.1, C35.1, C36.1, C42.1, C44.1, C64.1, C66.1, C70.1, CON3.1, R48.2, R49.2, R52.2, R53.2, R54.2, R65.2, R78.2, R80.2, R81.2, R82.2, U13.5, U14.5, U16.8, U18.10, U19.5; no longer C21.1, C25.1, C56.1, C61.1, C69.1, C71.1, C72.1, C74.1, CON6.1, R56.2, R59.2, R69.2, R71.2, R73.2, R75.2, R83.2, R85.2, R86.2, R88.2, R91.2, U15.10, U16.5, U21.8
- net 3V3_FB: now also R72.1, R73.2, U18.11; no longer R64.1, R65.2, U15.11
- net 3V3_SS: now also C61.1, U18.13; no longer C53.1, U15.13
- net 3V3_SW: now also U18.4; no longer U15.4
- net 4V2: now also C21.1, C52.1, C54.1, R59.2, R61.2, U18.17; no longer C19.1, C44.1, C46.1, R50.2, R52.2, U15.17
- net 4V2_EN: now also R58.2, U18.18, U2.9; no longer R49.2, U15.18
- net 4V2_FB: now also R61.1, R62.2, U18.16; no longer R52.1, R53.2, U15.16
- net 4V2_PGOOD: now also R65.1, U18.15, U2.95; no longer R56.1, U15.15
- net 4V2_SS: now also C57.1, U18.14; no longer C49.1, U15.14
- net 4V2_SW: now also U18.3; no longer U15.3
- net 4V2_VSENSE: now also C56.1, R59.1, R60.2, U2.47; no longer C48.1, R50.1, R51.2
- net 5V0: now also C40.1, C41.1, C45.1, C46.1, C48.1, C69.1, C75.1, C76.1, CON5.1, D4.1, R66.2, R89.2, U15.5, U18.1, U18.20, U18.6, U18.7, U18.9, U21.1, U21.12, U21.13, U21.14, U21.24; no longer C36.1, C37.1, C39.1, C58.1, C60.1, C67.1, C70.1, C73.1, CON4.1, D7.1, R57.2, R80.2, U13.5, U15.1, U15.20, U15.6, U15.7, U15.9, U17.1, U17.12, U17.13, U17.14, U17.24
- net 5V0_BACKUP: now also R77.2, U19.4; no longer R70.2, U16.4
- net 5V0_FB: now also R89.1, R90.2, U21.10, U21.18; no longer R80.1, R81.2, U17.10, U17.18
- net 5V0_ISENSE: now also C71.1, U2.50, U21.3; no longer C62.1, U17.3
- net 5V0_NBU: now also R86.1, U21.7; no longer R76.1, U17.7
- net 5V0_NBU_NSENS: now also C60.1, C63.1, C65.1, C67.1, R70.2, R74.2, R75.2, R86.2, U17.2, U21.16, U21.6; no longer C52.1, C55.1, C57.1, C59.1, R62.2, R66.2, R67.2, R76.2, U14.2, U17.16, U17.6
- net 5V0_NBU_NSENS_BST: now also C59.2, U17.7; no longer C51.2, U14.7
- net 5V0_NBU_NSENS_FB: now also C60.2, R70.1, R71.2, U17.19, U17.20; no longer C52.2, R62.1, R63.2, U14.19, U14.20
- net 5V0_NBU_NSENS_INTVCC: now also C53.1, U17.15, U17.3; no longer C45.1, U14.15, U14.3
- net 5V0_NBU_NSENS_PGOOD: now also R64.1, U17.1, U2.45; no longer R55.1, U14.1
- net 5V0_NBU_NSENS_RT: now also R63.2, U17.17; no longer R54.2, U14.17
- net 5V0_NBU_NSENS_SS: now also C55.1, U17.18; no longer C47.1, U14.18
- net 5V0_NBU_NSENS_SW: now also C59.1, U17.10, U17.8, U17.9; no longer C51.1, U14.10, U14.8, U14.9
- net 5V0_PGOOD: now also R80.1, U2.7, U21.11; no longer R72.1, U17.11
- net 5V0_VSENSE: now also C58.1, R66.1, R67.2, U2.48; no longer C50.1, R57.1, R58.2
- net BAT_CHRG_PROG: now also R83.2, U21.2; no longer R74.2, U17.2
- net BAT_OC: now also U22.3, U23.6; no longer U18.3, U20.6
- net BAT_OD: now also U22.1, U23.4; no longer U18.1, U20.4
- net BAT_PROT_CS: now also R88.2, U22.2; no longer R78.2, U18.2
- net BAT_PROT_VCC: now also R87.1, U22.5; no longer R77.1, U18.5
- net DCJACK_DET: now also CON3.5, R48.1, U2.92; no longer CON6.5, R69.1
- net GBAT: now also C72.2, CON6.2, U22.6, U23.3; no longer C64.2, CON2.2, U18.6, U20.3
- net GND: now also C51.2, C52.2, C64.2, C75.2, C76.2, CON2.2, CON3.6, CON4.3, CON5.5, D4.3, D5.A, D6.3, D7.C, D8.C, R47.1, R57.1, R60.1, R62.1, R67.1, R69.1, R71.1, R73.1, R76.1, R83.1, R88.1, R90.1, U14.3, U15.3, U16.4, U16.9, U17.12, U17.13, U17.21, U17.4, U17.M1, U17.M2, U17.M3, U17.M4, U18.19, U18.2, U18.21, U18.5, U18.8, U19.3, U20.2, U21.17, U21.25, U21.5, U23.1; no longer C59.2, C60.2, C72.2, CON3.2, CON4.5, CON5.3, CON6.6, D4.C, D5.C, D6.A, D7.3, D8.3, R48.1, R49.1, R51.1, R53.1, R54.1, R61.1, R65.1, R68.1, R74.1, R78.1, R81.1, R87.1, U14.12, U14.13, U14.21, U14.4, U14.5, U14.M1, U14.M2, U14.M3, U14.M4, U15.19, U15.2, U15.21, U15.5, U15.8, U16.3, U17.17, U17.25, U19.2, U20.1, U21.4, U21.9
- net GSM_LED_EN: now also U2.14
- net GSM_PWRKEY: now also U2.15
- net GSM_RF_SYNC: now also U2.18
- net GSM_STATUS: now also U2.21
- net I2C_SCL_USB_PD: now also CON3.3, R54.1, U16.2; no longer CON6.3, R85.1, U21.2
- net I2C_SDA_USB_PD: now also CON3.4, R53.1, U16.7; no longer CON6.4, R84.1, U21.7
- net LED_DI_BUF: now also U15.4; no longer U13.4
- net LED_DO: now also D4.4; no longer D7.4
- net MAG_ALERT: now also U2.99
- net N$37: now also U21.15; no longer U17.15
- net N$63: now also CON4.2, R51.2; no longer CON5.2, R90.2
- net N$64: now also CON4.1, R50.2; no longer CON5.1, R89.2
- net N$91: now also D7.A, R74.1; no longer D4.A, R66.1
- net N$92: now also D8.A, R77.1; no longer D5.A, R70.1
- net PF_THRESH: now also R75.1, R76.2, U21.19; no longer R67.1, R68.2, U17.19
- net RFM_IRQ: now also U2.6
- net RFM_RESET: now also U2.5
- net SIM_DATA: now also C25.1; no longer C24.1
- net SIM_VDD: now also C24.1; no longer C22.1
- net TIM3_CC2_BUZZ: now also U2.100
- net U0_CTS_GSM: now also U2.39
- net U0_RTS_GSM: now also U2.40
- net U0_RX_GSM: now also U2.38
- net U0_TX_GSM: now also U2.37
- net US0_CLK_WIFI: now also U2.69
- net US0_MISO_WIFI: now also U2.70
- net US0_MOSI_WIFI: now also U2.71
- net US2_CLK_TFT: now also U2.28
- net US2_MISO_TFT: now also U2.27
- net US2_MOSI_TFT: now also U2.26
- net US3_CLK_RFM: now also U2.3
- net US3_MISO_RFM: now also U2.2
- net US3_MOSI_RFM: now also U2.1
- net USB_D+: now also D6.1, R50.1; no longer D8.1, R89.1
- net USB_D-: now also D6.2, R51.1; no longer D8.2, R90.1
- net USB_PD_I2C_EN: now also R47.2, U16.1, U2.62; no longer R87.2, U21.1
- net USB_PD_I2C_READY: now also R52.1, U16.5, U2.63; no longer R86.1, U21.5
- net USB_VBUS_HV_STAT: now also CON5.2, R55.1, U2.86; no longer CON4.2, R91.1
- net USB_VBUS_SUP_EN: now also CON5.4, U2.93; no longer CON4.4
- net VBAT: now also C72.1, C73.1, C74.1, R68.2, R85.2, R87.2, U20.1, U21.23; no longer C64.1, C65.1, C66.1, R60.2, R77.2, R82.2, U17.23, U19.1
- net VBAT_NSENS: now also CON6.1, R85.1, U20.6; no longer CON2.1, R82.1, U19.6
- net VBAT_SW: now also U21.21, U21.22; no longer U17.21, U17.22
- net VBAT_VSENSE: now also C62.1, R68.1, R69.2, U2.49; no longer C54.1, R60.1, R61.2
- net VIN: now also C47.1, C49.1, C51.1, D5.C, R56.2, U17.11, U17.14, U17.6; no longer C40.1, C42.1, C63.1, D6.C, R47.2, U14.11, U14.14, U14.6
- net VIN_UNFUSED: now also CON2.1; no longer CON3.1
- net VIN_VSENSE: now also C50.1, R56.1, R57.2, U2.46; no longer C41.1, R47.1, R48.2
- net WIFI_EN: now also U2.66
- net WIFI_IRQ: now also U2.67
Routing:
- net SIM_VDD: track 0.00 -> 70.0 mm, vias 0 -> 2
- net SIM_CLK_FILT: track 0.00 -> 46.3 mm, vias 0 -> 2
- net SIM_RST_FILT: track 0.00 -> 46.0 mm, vias 0 -> 2
- net SIM_DATA_FILT: track 0.00 -> 27.3 mm, vias 0 -> 2
- net 3V3: track 49.8 -> 72.8 mm
- net GND: track 3.86 -> 22.1 mm
- net SIM_RST: track 0.00 -> 14.6 mm
- net SIM_CLK: track 0.00 -> 12.7 mm
- net SIM_DATA: track 0.00 -> 12.6 mm
- net BUZZ_DRV: track 0.00 -> 10.3 mm, vias 0 -> 1
- net QSPI_CS0: track 21.7 -> 26.2 mm
- net N$34: track 0.00 -> 4.38 mm
- net N$29: track 0.00 -> 2.93 mm
- net N$16: track 0.00 -> 2.73 mm
